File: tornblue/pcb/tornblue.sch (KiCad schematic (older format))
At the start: 78 parts, among them J1 BATT, J2 SWD, J3 BREAKOUT, J4 USB C - USB2.0, Q1 AO3401A, Q2 AO3401A, SW1 SW_Push, SW10 SW_Push, SW11 SW_Push, SW12 SW_Push, SW13 SW_Push, SW14 SW_Push, SW15 SW_Push, SW16 SW_Push, SW17 SW_Push, SW18 SW_Push, SW19 EC11, SW2 SW_Push, SW20 SW_Push, SW21 SW_Push, SW22 EC11, SW23 RESET, SW3 SW_Push, SW4 SW_Push, SW5 SW_Push, SW6 SW_Push, SW7 SW_Push, SW8 SW_Push, SW9 SW_Push, U1 XC6220, U2 TP4056, U3 nRF52840_holyiot_18010, U4 SRV05-4

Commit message: Removed support for Kailh MX sockets
It is not possible to include options for Kailh MX sockets, underglow
LEDS and Panasonic EVQWGD001 encoder on the same PCB.
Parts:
- H1, H2, H3, H4: footprint MountingHole:MountingHole_2.7mm_M2.5_DIN965_Pad -> MountingHole:MountingHole_3.2mm_M3_DIN965_Pad
- H5, H6: footprint tornblue:MountingHole_2.7mm_M2.5_DIN965_Pad_Slot -> tornblue:MountingHole_3.2mm_M3_DIN965_Pad_Slot
- SW1, SW10, SW11, SW12, SW13, SW14, SW15, SW16, SW17, SW18, SW2, SW20, SW21, SW3, SW4, SW5, SW6, SW7, SW8, SW9: footprint tornblue:Kailh_socket_MX_PG1350_optional_reversible -> tornblue:MX_PG1350_optional
- SW23: footprint tornblue:SW_SPST_TS-1012E-26 -> tornblue:SW_SPST_TS24CA; LCSC C455253 -> C393942
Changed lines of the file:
@@
 F 0 "SW23" H 9900 3550 50  0000 C CNN
 F 1 "RESET" H 9900 3650 50  0000 C CNN
-F 2 "tornblue:SW_SPST_TS-1012E-26" H 9900 3950 50  0001 C CNN
-F 3 "https://datasheet.lcsc.com/lcsc/1912111437_XUNPU-TS-1012E-26_C455253.pdf" H 9900 3950 50  0001 C CNN
-F 4 "C455253" H 9900 3750 50  0001 C CNN "LCSC"
+F 2 "tornblue:SW_SPST_TS24CA" H 9900 3950 50  0001 C CNN
+F 3 "https://datasheet.lcsc.com/lcsc/1912111437_SHOU-HAN-TS24CA_C393942.pdf" H 9900 3950 50  0001 C CNN
+F 4 "C393942" H 9900 3750 50  0001 C CNN "LCSC"
 	1    9900 3750
 	1    0    0    -1
@@
 F 0 "SW5" H 3200 4585 50  0000 C CNN
 F 1 "SW_Push" H 3200 4494 50  0000 C CNN
-F 2 "tornblue:Kailh_socket_MX_PG1350_optional_reversible" H 3200 4500 50  0001 C CNN
+F 2 "tornblue:MX_PG1350_optional" H 3200 4500 50  0001 C CNN
 F 3 "~" H 3200 4500 50  0001 C CNN
 F 4 "-" H 3200 4300 50  0001 C CNN "LCSC"
@@
 F 0 "SW6" H 4350 4585 50  0000 C CNN
 F 1 "SW_Push" H 4350 4494 50  0000 C CNN
-F 2 "tornblue:Kailh_socket_MX_PG1350_optional_reversible" H 4350 4500 50  0001 C CNN
+F 2 "tornblue:MX_PG1350_optional" H 4350 4500 50  0001 C CNN
 F 3 "~" H 4350 4500 50  0001 C CNN
 F 4 "-" H 4350 4300 50  0001 C CNN "LCSC"
@@
 F 0 "SW11" H 3200 5335 50  0000 C CNN
 F 1 "SW_Push" H 3200 5244 50  0000 C CNN
-F 2 "tornblue:Kailh_socket_MX_PG1350_optional_reversible" H 3200 5250 50  0001 C CNN
+F 2 "tornblue:MX_PG1350_optional" H 3200 5250 50  0001 C CNN
 F 3 "~" H 3200 5250 50  0001 C CNN
 F 4 "-" H 3200 5050 50  0001 C CNN "LCSC"
@@
 F 0 "SW12" H 4350 5335 50  0000 C CNN
 F 1 "SW_Push" H 4350 5244 50  0000 C CNN
-F 2 "tornblue:Kailh_socket_MX_PG1350_optional_reversible" H 4350 5250 50  0001 C CNN
+F 2 "tornblue:MX_PG1350_optional" H 4350 5250 50  0001 C CNN
 F 3 "~" H 4350 5250 50  0001 C CNN
 F 4 "-" H 4350 5050 50  0001 C CNN "LCSC"
@@
 F 0 "SW17" H 3200 6085 50  0000 C CNN
 F 1 "SW_Push" H 3200 5994 50  0000 C CNN
-F 2 "tornblue:Kailh_socket_MX_PG1350_optional_reversible" H 3200 6000 50  0001 C CNN
+F 2 "tornblue:MX_PG1350_optional" H 3200 6000 50  0001 C CNN
 F 3 "~" H 3200 6000 50  0001 C CNN
 F 4 "-" H 3200 5800 50  0001 C CNN "LCSC"
@@
 F 0 "SW18" H 4350 6085 50  0000 C CNN
 F 1 "SW_Push" H 4350 5994 50  0000 C CNN
-F 2 "tornblue:Kailh_socket_MX_PG1350_optional_reversible" H 4350 6000 50  0001 C CNN
+F 2 "tornblue:MX_PG1350_optional" H 4350 6000 50  0001 C CNN
 F 3 "~" H 4350 6000 50  0001 C CNN
 F 4 "-" H 4350 5800 50  0001 C CNN "LCSC"
@@
 F 0 "H1" H 950 2846 50  0000 L CNN
 F 1 "MountingHole" H 950 2755 50  0001 L CNN
-F 2 "MountingHole:MountingHole_2.7mm_M2.5_DIN965_Pad" H 850 2800 50  0001 C CNN
+F 2 "MountingHole:MountingHole_3.2mm_M3_DIN965_Pad" H 850 2800 50  0001 C CNN
 F 3 "~" H 850 2800 50  0001 C CNN
 F 4 "-" H 850 2800 50  0001 C CNN "LCSC"
@@
 F 0 "H2" H 950 3046 50  0000 L CNN
 F 1 "MountingHole" H 950 2955 50  0001 L CNN
-F 2 "MountingHole:MountingHole_2.7mm_M2.5_DIN965_Pad" H 850 3000 50  0001 C CNN
+F 2 "MountingHole:MountingHole_3.2mm_M3_DIN965_Pad" H 850 3000 50  0001 C CNN
 F 3 "~" H 850 3000 50  0001 C CNN
 F 4 "-" H 850 3000 50  0001 C CNN "LCSC"
@@
 F 0 "H3" H 950 3246 50  0000 L CNN
 F 1 "MountingHole" H 950 3155 50  0001 L CNN
-F 2 "MountingHole:MountingHole_2.7mm_M2.5_DIN965_Pad" H 850 3200 50  0001 C CNN
+F 2 "MountingHole:MountingHole_3.2mm_M3_DIN965_Pad" H 850 3200 50  0001 C CNN
 F 3 "~" H 850 3200 50  0001 C CNN
 F 4 "-" H 850 3200 50  0001 C CNN "LCSC"
@@
 F 0 "H6" H 1300 3246 50  0000 L CNN
 F 1 "MountingHole" H 1300 3155 50  0001 L CNN
-F 2 "tornblue:MountingHole_2.7mm_M2.5_DIN965_Pad_Slot" H 1200 3200 50  0001 C CNN
+F 2 "tornblue:MountingHole_3.2mm_M3_DIN965_Pad_Slot" H 1200 3200 50  0001 C CNN
 F 3 "~" H 1200 3200 50  0001 C CNN
 F 4 "-" H 1200 3200 50  0001 C CNN "LCSC"
@@
 F 0 "H5" H 1300 3046 50  0000 L CNN
 F 1 "MountingHole" H 1300 2955 50  0001 L CNN
-F 2 "tornblue:MountingHole_2.7mm_M2.5_DIN965_Pad_Slot" H 1200 3000 50  0001 C CNN
+F 2 "tornblue:MountingHole_3.2mm_M3_DIN965_Pad_Slot" H 1200 3000 50  0001 C CNN
 F 3 "~" H 1200 3000 50  0001 C CNN
 F 4 "-" H 1200 3000 50  0001 C CNN "LCSC"
@@
 F 0 "H4" H 1300 2846 50  0000 L CNN
 F 1 "MountingHole" H 1300 2755 50  0001 L CNN
-F 2 "MountingHole:MountingHole_2.7mm_M2.5_DIN965_Pad" H 1200 2800 50  0001 C CNN
+F 2 "MountingHole:MountingHole_3.2mm_M3_DIN965_Pad" H 1200 2800 50  0001 C CNN
 F 3 "~" H 1200 2800 50  0001 C CNN
 F 4 "-" H 1200 2800 50  0001 C CNN "LCSC"
@@
 F 0 "SW4" H 2100 4585 50  0000 C CNN
 F 1 "SW_Push" H 2100 4494 50  0000 C CNN
-F 2 "tornblue:Kailh_socket_MX_PG1350_optional_reversible" H 2100 4500 50  0001 C CNN
+F 2 "tornblue:MX_PG1350_optional" H 2100 4500 50  0001 C CNN
 F 3 "~" H 2100 4500 50  0001 C CNN
 F 4 "-" H 2100 4300 50  0001 C CNN "LCSC"
@@
 F 0 "SW10" H 2100 5335 50  0000 C CNN
 F 1 "SW_Push" H 2100 5244 50  0000 C CNN
-F 2 "tornblue:Kailh_socket_MX_PG1350_optional_reversible" H 2100 5250 50  0001 C CNN
+F 2 "tornblue:MX_PG1350_optional" H 2100 5250 50  0001 C CNN
 F 3 "~" H 2100 5250 50  0001 C CNN
 F 4 "-" H 2100 5050 50  0001 C CNN "LCSC"
@@
 F 0 "SW16" H 2100 6085 50  0000 C CNN
 F 1 "SW_Push" H 2100 5994 50  0000 C CNN
-F 2 "tornblue:Kailh_socket_MX_PG1350_optional_reversible" H 2100 6000 50  0001 C CNN
+F 2 "tornblue:MX_PG1350_optional" H 2100 6000 50  0001 C CNN
 F 3 "~" H 2100 6000 50  0001 C CNN
 F 4 "-" H 2100 5800 50  0001 C CNN "LCSC"
@@
 F 0 "SW9" H 1550 5335 50  0000 C CNN
 F 1 "SW_Push" H 1550 5244 50  0000 C CNN
-F 2 "tornblue:Kailh_socket_MX_PG1350_optional_reversible" H 1550 5250 50  0001 C CNN
+F 2 "tornblue:MX_PG1350_optional" H 1550 5250 50  0001 C CNN
 F 3 "~" H 1550 5250 50  0001 C CNN
 F 4 "-" H 1550 5050 50  0001 C CNN "LCSC"
@@
 F 0 "SW20" H 2050 7385 50  0000 C CNN
 F 1 "SW_Push" H 2050 7294 50  0000 C CNN
-F 2 "tornblue:Kailh_socket_MX_PG1350_optional_reversible" H 2050 7300 50  0001 C CNN
+F 2 "tornblue:MX_PG1350_optional" H 2050 7300 50  0001 C CNN
 F 3 "~" H 2050 7300 50  0001 C CNN
 F 4 "-" H 2050 7100 50  0001 C CNN "LCSC"
@@
 F 0 "SW15" H 1550 6085 50  0000 C CNN
 F 1 "SW_Push" H 1550 5994 50  0000 C CNN
-F 2 "tornblue:Kailh_socket_MX_PG1350_optional_reversible" H 1550 6000 50  0001 C CNN
+F 2 "tornblue:MX_PG1350_optional" H 1550 6000 50  0001 C CNN
 F 3 "~" H 1550 6000 50  0001 C CNN
 F 4 "-" H 1550 5800 50  0001 C CNN "LCSC"
@@
 F 0 "SW3" H 1550 4585 50  0000 C CNN
 F 1 "SW_Push" H 1550 4494 50  0000 C CNN
-F 2 "tornblue:Kailh_socket_MX_PG1350_optional_reversible" H 1550 4500 50  0001 C CNN
+F 2 "tornblue:MX_PG1350_optional" H 1550 4500 50  0001 C CNN
 F 3 "~" H 1550 4500 50  0001 C CNN
 F 4 "-" H 1550 4300 50  0001 C CNN "LCSC"
@@
 F 0 "SW14" H 2650 6085 50  0000 C CNN
 F 1 "SW_Push" H 2650 5994 50  0000 C CNN
-F 2 "tornblue:Kailh_socket_MX_PG1350_optional_reversible" H 2650 6000 50  0001 C CNN
+F 2 "tornblue:MX_PG1350_optional" H 2650 6000 50  0001 C CNN
 F 3 "~" H 2650 6000 50  0001 C CNN
 F 4 "-" H 2650 5800 50  0001 C CNN "LCSC"
@@
 F 0 "SW8" H 2650 5335 50  0000 C CNN
 F 1 "SW_Push" H 2650 5244 50  0000 C CNN
-F 2 "tornblue:Kailh_socket_MX_PG1350_optional_reversible" H 2650 5250 50  0001 C CNN
+F 2 "tornblue:MX_PG1350_optional" H 2650 5250 50  0001 C CNN
 F 3 "~" H 2650 5250 50  0001 C CNN
 F 4 "-" H 2650 5050 50  0001 C CNN "LCSC"
@@
 F 0 "SW2" H 2650 4585 50  0000 C CNN
 F 1 "SW_Push" H 2650 4494 50  0000 C CNN
-F 2 "tornblue:Kailh_socket_MX_PG1350_optional_reversible" H 2650 4500 50  0001 C CNN
+F 2 "tornblue:MX_PG1350_optional" H 2650 4500 50  0001 C CNN
 F 3 "~" H 2650 4500 50  0001 C CNN
 F 4 "-" H 2650 4300 50  0001 C CNN "LCSC"
@@
 F 0 "SW1" H 3750 4585 50  0000 C CNN
 F 1 "SW_Push" H 3750 4494 50  0000 C CNN
-F 2 "tornblue:Kailh_socket_MX_PG1350_optional_reversible" H 3750 4500 50  0001 C CNN
+F 2 "tornblue:MX_PG1350_optional" H 3750 4500 50  0001 C CNN
 F 3 "~" H 3750 4500 50  0001 C CNN
 F 4 "-" H 3750 4300 50  0001 C CNN "LCSC"
@@
 F 0 "SW7" H 3750 5335 50  0000 C CNN
 F 1 "SW_Push" H 3750 5244 50  0000 C CNN
-F 2 "tornblue:Kailh_socket_MX_PG1350_optional_reversible" H 3750 5250 50  0001 C CNN
+F 2 "tornblue:MX_PG1350_optional" H 3750 5250 50  0001 C CNN
 F 3 "~" H 3750 5250 50  0001 C CNN
 F 4 "-" H 3750 5050 50  0001 C CNN "LCSC"
@@
 F 0 "SW13" H 3750 6085 50  0000 C CNN
 F 1 "SW_Push" H 3750 5994 50  0000 C CNN
-F 2 "tornblue:Kailh_socket_MX_PG1350_optional_reversible" H 3750 6000 50  0001 C CNN
+F 2 "tornblue:MX_PG1350_optional" H 3750 6000 50  0001 C CNN
 F 3 "~" H 3750 6000 50  0001 C CNN
 F 4 "-" H 3750 5800 50  0001 C CNN "LCSC"
@@
 F 0 "SW21" H 3750 7385 50  0000 C CNN
 F 1 "SW_Push" H 3750 7294 50  0000 C CNN
-F 2 "tornblue:Kailh_socket_MX_PG1350_optional_reversible" H 3750 7300 50  0001 C CNN
+F 2 "tornblue:MX_PG1350_optional" H 3750 7300 50  0001 C CNN
 F 3 "~" H 3750 7300 50  0001 C CNN
 F 4 "-" H 3750 7100 50  0001 C CNN "LCSC"

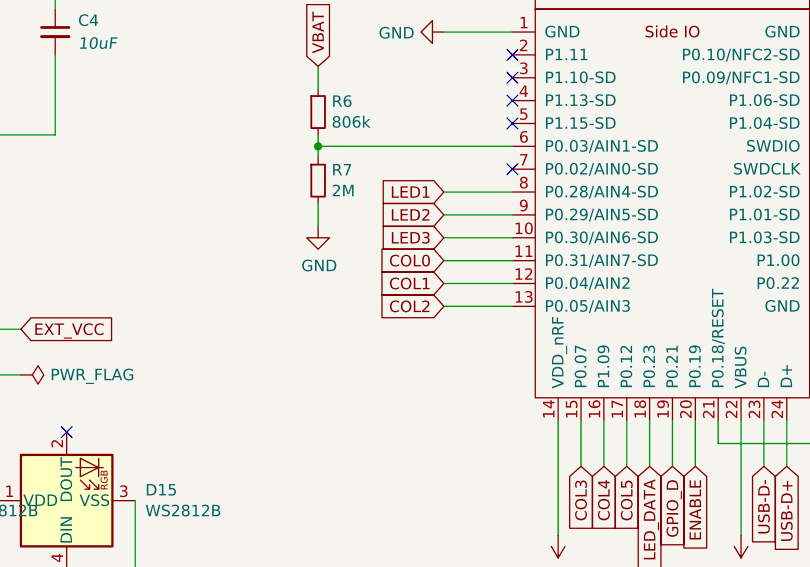
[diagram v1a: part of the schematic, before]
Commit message: Move holyiot module up 1.5mm
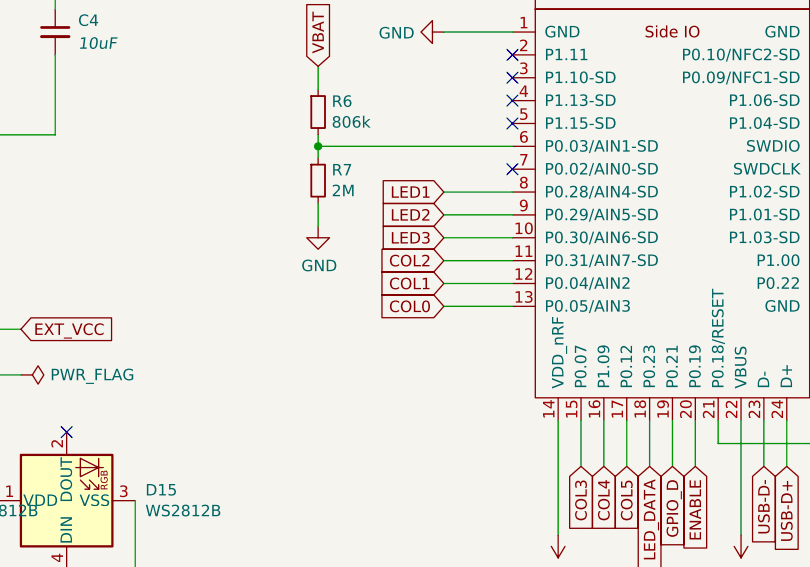
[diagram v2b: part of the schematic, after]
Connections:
- net COL0: now also U3.13 (P0.05/AIN3); no longer U3.11 (P0.31/AIN7-SD)
- net COL2: now also U3.11 (P0.31/AIN7-SD); no longer U3.13 (P0.05/AIN3)
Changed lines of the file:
@@
 Text GLabel 9750 2250 2    50   Input ~ 0
 ROW3
+Text GLabel 7800 3150 0    50   Input ~ 0
+COL0
 Text GLabel 7800 2950 0    50   Input ~ 0
-COL0
-Text GLabel 7800 3150 0    50   Input ~ 0
 COL2
 Text GLabel 8400 3850 3    50   Input ~ 0

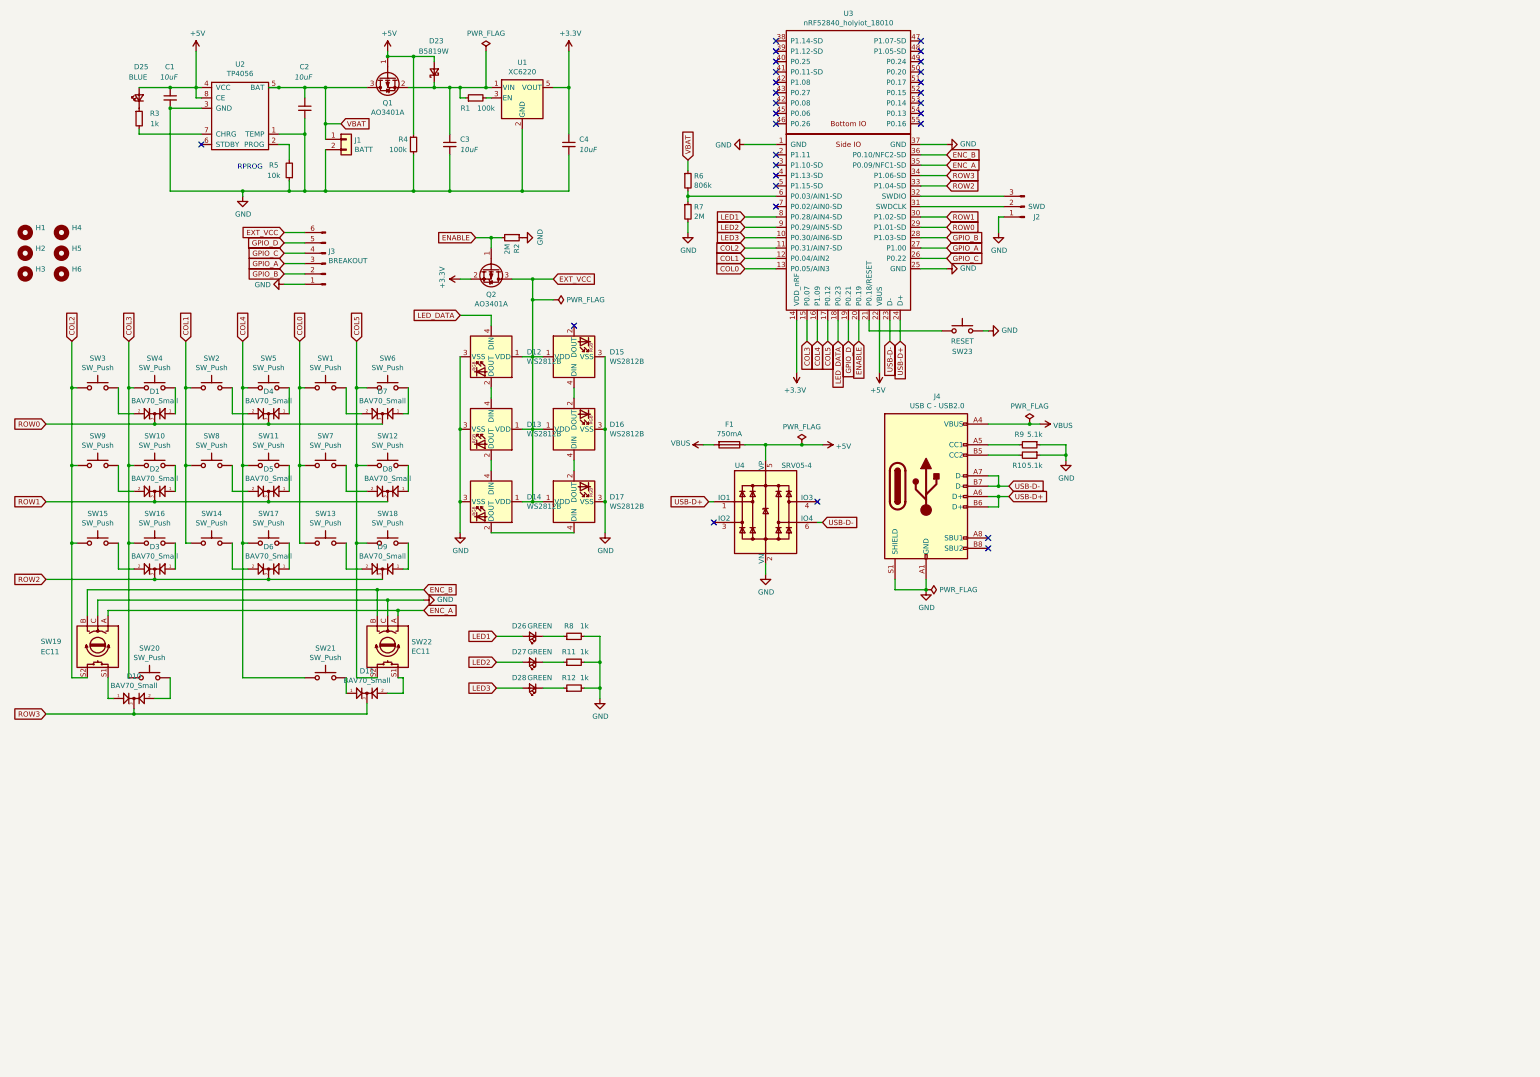
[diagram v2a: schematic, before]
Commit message: Rearrange BAV70 grid
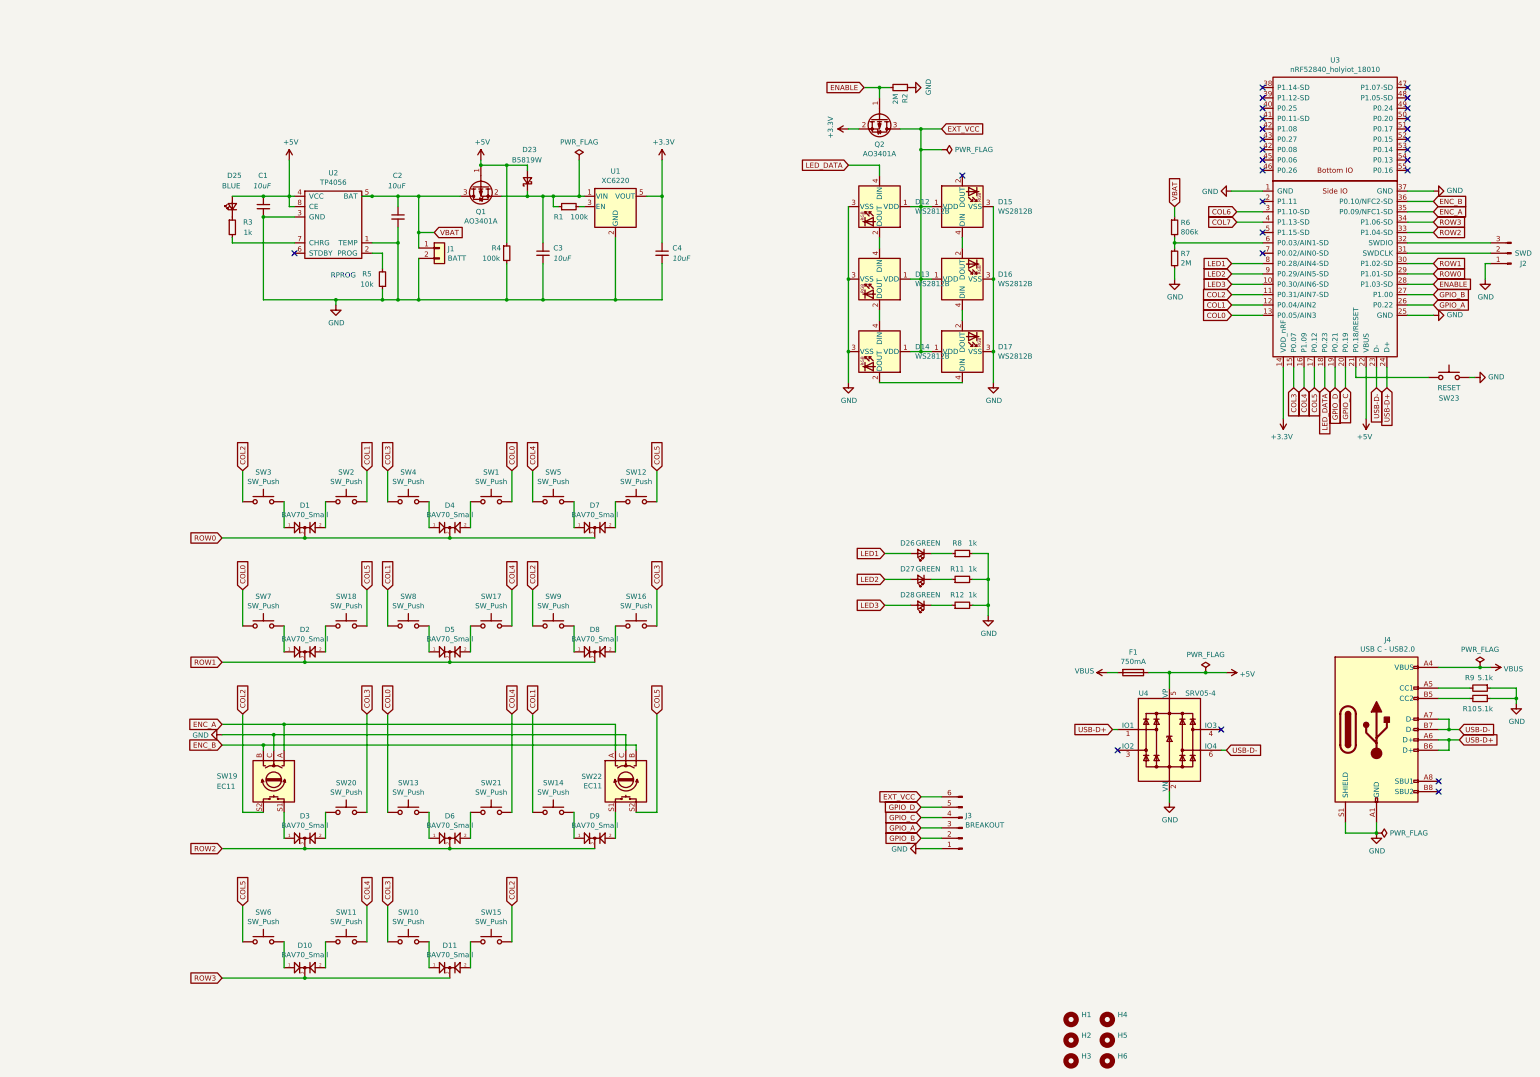
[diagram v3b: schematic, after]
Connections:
- net ENABLE: now also U3.28 (P1.03-SD); no longer U3.20 (P0.19)
- net GPIO_A: now also U3.26 (P0.22); no longer U3.27 (P1.00)
- net GPIO_B: now also U3.27 (P1.00); no longer U3.28 (P1.03-SD)
- net GPIO_C: now also U3.20 (P0.19); no longer U3.26 (P0.22)
- net COL6: now reaches U3.3 (P1.10-SD)
- net COL7: now reaches U3.4 (P1.13-SD)
- net at SW3.2: now also D1.1 (A1); no longer D1.2 (A2)
- net at SW4.2: now also D4.1 (A1); no longer D1.1 (A1)
- net at SW2.2: now also D1.2 (A2); no longer D4.2 (A2)
- net at SW5.2: now also D7.1 (A1); no longer D4.1 (A1)
- net at SW1.2: now also D4.2 (A2); no longer D7.2 (A2)
- net at SW6.2: now also D10.1 (A1); no longer D7.1 (A1)
- net at SW9.2: now also D8.1 (A1); no longer D2.2 (A2)
- net at SW10.2: now also D11.1 (A1); no longer D2.1 (A1)
- net at SW8.2: now also D5.1 (A1); no longer D5.2 (A2)
- net at SW11.2: now also D10.2 (A2); no longer D5.1 (A1)
- net at SW7.2: now also D2.1 (A1); no longer D8.2 (A2)
- net at SW12.2: now also D7.2 (A2); no longer D8.1 (A1)
- net at SW15.2: now also D11.2 (A2); no longer D3.2 (A2)
- net at SW16.2: now also D8.2 (A2); no longer D3.1 (A1)
- net at SW14.2: now also D9.1 (A1); no longer D6.2 (A2)
- net at SW17.2: now also D5.2 (A2); no longer D6.1 (A1)
- net at SW13.2: now also D6.1 (A1); no longer D9.2 (A2)
- net at SW18.2: now also D2.2 (A2); no longer D9.1 (A1)
- net at SW20.2: now also D3.2 (A2); no longer D10.2 (A2)
- net at SW21.2: now also D6.2 (A2); no longer D11.1 (A1)
- net at SW19.S1: now also D3.1 (A1); no longer D10.1 (A1)
- net at SW22.S1: now also D9.2 (A2); no longer D11.2 (A2)
- no-connect marks 29 -> 27
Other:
- moved on the sheet: C1, C2, C3, C4, D1, D10, D11, D12, D13, D14, D15, D16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

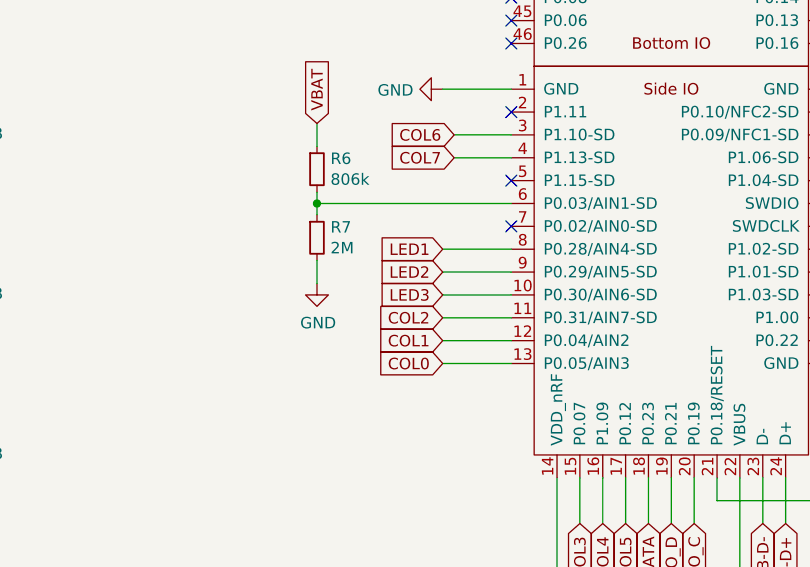
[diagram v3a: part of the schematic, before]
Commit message: Move BAV70 grid up 0.5mm
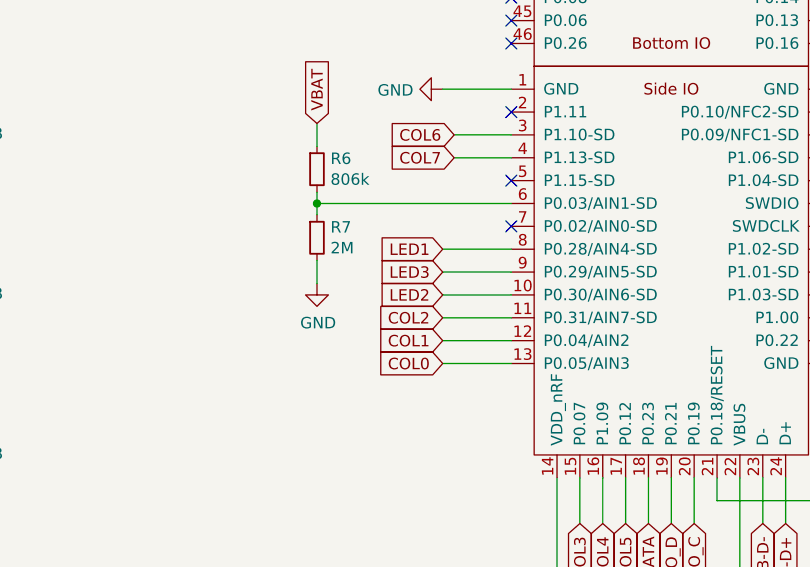
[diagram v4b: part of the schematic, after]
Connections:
- net LED2: now also U3.10 (P0.30/AIN6-SD); no longer U3.9 (P0.29/AIN5-SD)
- net LED3: now also U3.9 (P0.29/AIN5-SD); no longer U3.10 (P0.30/AIN6-SD)
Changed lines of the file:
@@
 Wire Wire Line
 	4200 2450 4450 2450
+Text GLabel 12500 3300 0    50   Input ~ 0
+LED2
 Text GLabel 12500 3200 0    50   Input ~ 0
-LED2
-Text GLabel 12500 3300 0    50   Input ~ 0
 LED3
 Wire Wire Line
